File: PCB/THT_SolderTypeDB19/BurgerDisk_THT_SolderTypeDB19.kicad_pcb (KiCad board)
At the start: 2 copper layers, 93.7 x 67.6 mm, 18 parts, among them J1 Daisy port in, J2 MicroSD module, J3 UART, J4 Daisy port out, U1 PC817

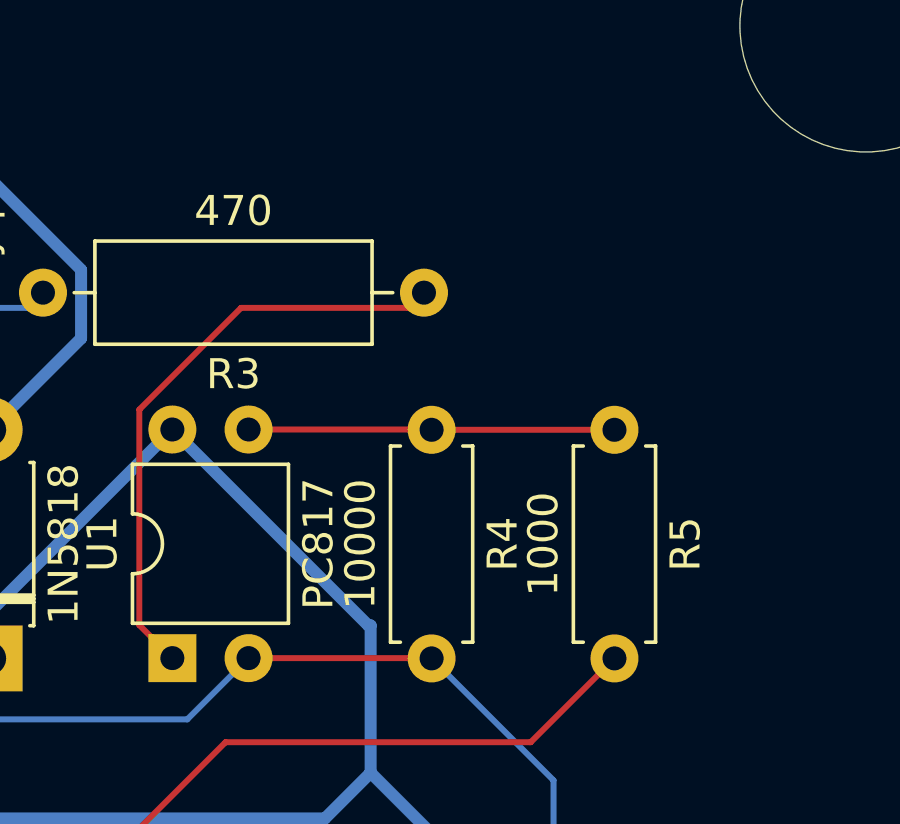
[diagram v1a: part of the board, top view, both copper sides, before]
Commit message: Reverse 3 resistors for correct silkscreen orientation
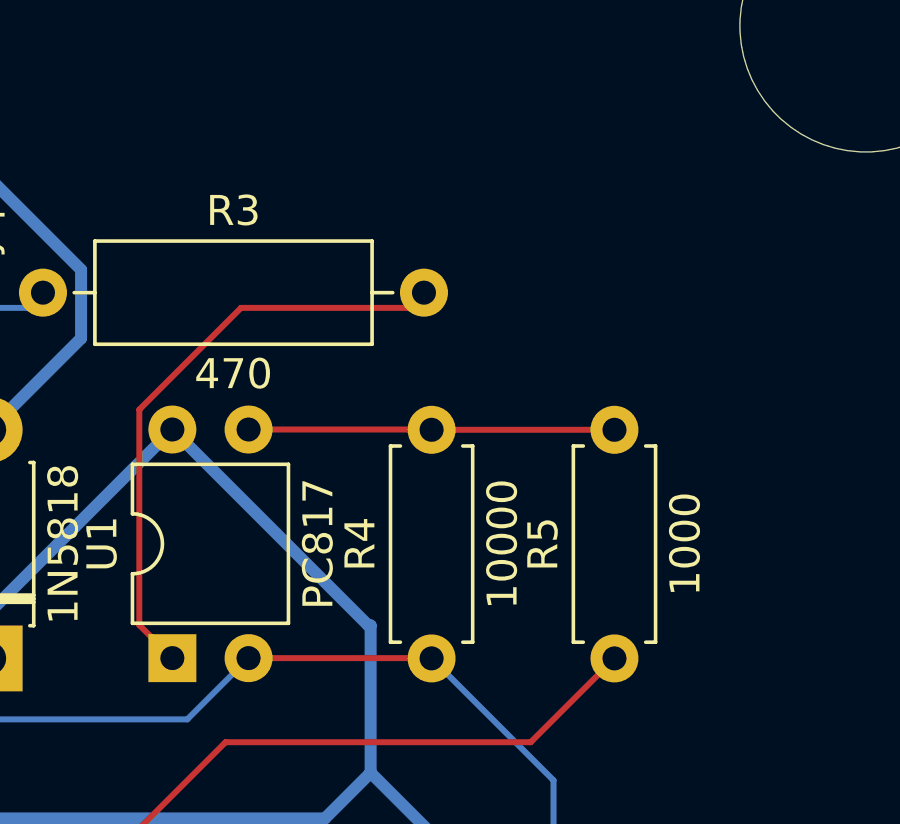
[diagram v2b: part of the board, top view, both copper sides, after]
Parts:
- moved R3 12.7 mm to (126.7, 72.9), turned to 0 degrees
- moved R4 7.62 mm to (139.7, 85.1), turned to 90 degrees
- moved R5 7.62 mm to (145.8, 85.1), turned to 90 degrees
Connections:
- R3 pad 1: Net-(R3-Pad1) -> DRV2_in
- R3 pad 2: DRV2_in -> Net-(R3-Pad2)
- R4 pad 1: Net-(R4-Pad1) -> GND
- R4 pad 2: GND -> Net-(R4-Pad2)
- R5 pad 1: Net-(R4-Pad1) -> DRV2_burgerDisk
- R5 pad 2: DRV2_burgerDisk -> Net-(R4-Pad2)
- U1 pad 1: Net-(R3-Pad1) -> Net-(R3-Pad2)
- U1 pad 3: Net-(R4-Pad1) -> Net-(R4-Pad2)
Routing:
- net Net-(R3-Pad2): track 0.00 -> 19.8 mm
- net Net-(R3-Pad1): track 19.8 -> 0.00 mm
- net Net-(R4-Pad2): track 0.00 -> 12.2 mm
- net Net-(R4-Pad1): track 12.2 -> 0.00 mm
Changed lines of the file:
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@@
   (net 36 "unconnected-(A1-A6-Pad25)")
   (net 37 "unconnected-(A1-3V3-Pad17)")
-  (net 38 "Net-(R4-Pad1)")
-  (net 39 "Net-(R3-Pad1)")
+  (net 38 "Net-(R3-Pad2)")
+  (net 39 "Net-(R4-Pad2)")
   (net 40 "HDSEL_in")
   (net 41 "Net-(D4-A)")
@@
       (stroke (width 0.1) (type solid)) (layer "F.Fab"))
     (pad "1" thru_hole rect (at 0 0 90) (size 1.6 1.6) (drill 0.8) (layers "*.Cu" "*.Mask")
-      (net 39 "Net-(R3-Pad1)") (pintype "passive"))
+      (net 38 "Net-(R3-Pad2)") (pintype "passive"))
     (pad "2" thru_hole oval (at 0 2.54 90) (size 1.6 1.6) (drill 0.8) (layers "*.Cu" "*.Mask")
       (net 2 "GND") (pintype "passive"))
     (pad "3" thru_hole oval (at 7.62 2.54 90) (size 1.6 1.6) (drill 0.8) (layers "*.Cu" "*.Mask")
-      (net 38 "Net-(R4-Pad1)") (pintype "passive"))
+      (net 39 "Net-(R4-Pad2)") (pintype "passive"))
     (pad "4" thru_hole oval (at 7.62 0 90) (size 1.6 1.6) (drill 0.8) (layers "*.Cu" "*.Mask")
       (net 20 "5V_burgerDisk") (pintype "passive"))
@@
   )
   (footprint "Resistor_THT:R_Axial_DIN0309_L9.0mm_D3.2mm_P12.70mm_Horizontal" (layer "F.Cu")
-    (at 139.446 72.898 180)
+    (at 126.746 72.898)
     (descr "Resistor, Axial_DIN0309 series, Axial, Horizontal, pin pitch=12.7mm, 0.5W = 1/2W, length*diameter=9*3.2mm^2, http://cdn-reichelt.de/documents/datenblatt/B400/1_4W%23YAG.pdf")
     (tags "Resistor Axial_DIN0309 series Axial Horizontal pin pitch 12.7mm 0.5W = 1/2W length 9mm diameter 3.2mm")
@@
     (fp_line (start 12.7 0) (end 10.85 0)
       (stroke (width 0.1) (type solid)) (layer "F.Fab"))
-    (pad "1" thru_hole circle (at 0 0 180) (size 1.6 1.6) (drill 0.8) (layers "*.Cu" "*.Mask")
-      (net 39 "Net-(R3-Pad1)") (pintype "passive"))
-    (pad "2" thru_hole oval (at 12.7 0 180) (size 1.6 1.6) (drill 0.8) (layers "*.Cu" "*.Mask")
+    (pad "1" thru_hole circle (at 0 0) (size 1.6 1.6) (drill 0.8) (layers "*.Cu" "*.Mask")
       (net 27 "DRV2_in") (pintype "passive"))
+    (pad "2" thru_hole oval (at 12.7 0) (size 1.6 1.6) (drill 0.8) (layers "*.Cu" "*.Mask")
+      (net 38 "Net-(R3-Pad2)") (pintype "passive"))
     (model "${KICAD6_3DMODEL_DIR}/Resistor_THT.3dshapes/R_Axial_DIN0309_L9.0mm_D3.2mm_P12.70mm_Horizontal.wrl"
       (offset (xyz 0 0 0))
@@
   )
   (footprint "Resistor_THT:R_Axial_DIN0207_L6.3mm_D2.5mm_P7.62mm_Horizontal" (layer "F.Cu")
-    (at 139.7 77.47 -90)
+    (at 139.7 85.09 90)
     (descr "Resistor, Axial_DIN0207 series, Axial, Horizontal, pin pitch=7.62mm, 0.25W = 1/4W, length*diameter=6.3*2.5mm^2, http://cdn-reichelt.de/documents/datenblatt/B400/1_4W%23YAG.pdf")
     (tags "Resistor Axial_DIN0207 series Axial Horizontal pin pitch 7.62mm 0.25W = 1/4W length 6.3mm diameter 2.5mm")
@@
     (fp_line (start 7.62 0) (end 6.96 0)
       (stroke (width 0.1) (type solid)) (layer "F.Fab"))
-    (pad "1" thru_hole circle (at 0 0 270) (size 1.6 1.6) (drill 0.8) (layers "*.Cu" "*.Mask")
-      (net 38 "Net-(R4-Pad1)") (pintype "passive"))
-    (pad "2" thru_hole oval (at 7.62 0 270) (size 1.6 1.6) (drill 0.8) (layers "*.Cu" "*.Mask")
+    (pad "1" thru_hole circle (at 0 0 90) (size 1.6 1.6) (drill 0.8) (layers "*.Cu" "*.Mask")
       (net 2 "GND") (pintype "passive"))
+    (pad "2" thru_hole oval (at 7.62 0 90) (size 1.6 1.6) (drill 0.8) (layers "*.Cu" "*.Mask")
+      (net 39 "Net-(R4-Pad2)") (pintype "passive"))
     (model "${KICAD6_3DMODEL_DIR}/Resistor_THT.3dshapes/R_Axial_DIN0207_L6.3mm_D2.5mm_P7.62mm_Horizontal.wrl"
       (offset (xyz 0 0 0))
@@
   )
   (footprint "Resistor_THT:R_Axial_DIN0207_L6.3mm_D2.5mm_P7.62mm_Horizontal" (layer "F.Cu")
-    (at 145.796 77.47 -90)
+    (at 145.796 85.09 90)
     (descr "Resistor, Axial_DIN0207 series, Axial, Horizontal, pin pitch=7.62mm, 0.25W = 1/4W, length*diameter=6.3*2.5mm^2, http://cdn-reichelt.de/documents/datenblatt/B400/1_4W%23YAG.pdf")
     (tags "Resistor Axial_DIN0207 series Axial Horizontal pin pitch 7.62mm 0.25W = 1/4W length 6.3mm diameter 2.5mm")
@@
     (fp_line (start 7.62 0) (end 6.96 0)
       (stroke (width 0.1) (type solid)) (layer "F.Fab"))
-    (pad "1" thru_hole circle (at 0 0 270) (size 1.6 1.6) (drill 0.8) (layers "*.Cu" "*.Mask")
-      (net 38 "Net-(R4-Pad1)") (pintype "passive"))
-    (pad "2" thru_hole oval (at 7.62 0 270) (size 1.6 1.6) (drill 0.8) (layers "*.Cu" "*.Mask")
+    (pad "1" thru_hole circle (at 0 0 90) (size 1.6 1.6) (drill 0.8) (layers "*.Cu" "*.Mask")
       (net 10 "DRV2_burgerDisk") (pintype "passive"))
+    (pad "2" thru_hole oval (at 7.62 0 90) (size 1.6 1.6) (drill 0.8) (layers "*.Cu" "*.Mask")
+      (net 39 "Net-(R4-Pad2)") (pintype "passive"))
     (model "${KICAD6_3DMODEL_DIR}/Resistor_THT.3dshapes/R_Axial_DIN0207_L6.3mm_D2.5mm_P7.62mm_Horizontal.wrl"
       (offset (xyz 0 0 0))
@@
   (segment (start 139.192 50.8) (end 140.965 49.027) (width 0.2) (layer "B.Cu") (net 28))
   (segment (start 140.965 49.027) (end 140.965 45.72) (width 0.2) (layer "B.Cu") (net 28))
-  (segment (start 139.69 77.46) (end 139.7 77.47) (width 0.2) (layer "F.Cu") (net 38))
-  (segment (start 139.7 77.47) (end 145.796 77.47) (width 0.2) (layer "F.Cu") (net 38))
-  (segment (start 133.599 77.46) (end 139.69 77.46) (width 0.2) (layer "F.Cu") (net 38))
-  (segment (start 129.959 83.98) (end 129.959 76.797) (width 0.2) (layer "F.Cu") (net 39))
-  (segment (start 131.059 85.08) (end 129.959 83.98) (width 0.2) (layer "F.Cu") (net 39))
-  (segment (start 138.938 73.406) (end 139.446 72.898) (width 0.2) (layer "F.Cu") (net 39))
-  (segment (start 129.959 76.797) (end 133.35 73.406) (width 0.2) (layer "F.Cu") (net 39))
-  (segment (start 133.35 73.406) (end 138.938 73.406) (width 0.2) (layer "F.Cu") (net 39))
+  (segment (start 129.959 83.98) (end 129.959 76.797) (width 0.2) (layer "F.Cu") (net 38))
+  (segment (start 131.059 85.08) (end 129.959 83.98) (width 0.2) (layer "F.Cu") (net 38))
+  (segment (start 138.938 73.406) (end 139.446 72.898) (width 0.2) (layer "F.Cu") (net 38))
+  (segment (start 129.959 76.797) (end 133.35 73.406) (width 0.2) (layer "F.Cu") (net 38))
+  (segment (start 133.35 73.406) (end 138.938 73.406) (width 0.2) (layer "F.Cu") (net 38))
+  (segment (start 139.69 77.46) (end 139.7 77.47) (width 0.2) (layer "F.Cu") (net 39))
+  (segment (start 139.7 77.47) (end 145.796 77.47) (width 0.2) (layer "F.Cu") (net 39))
+  (segment (start 133.599 77.46) (end 139.69 77.46) (width 0.2) (layer "F.Cu") (net 39))
   (segment (start 108.458 68.834) (end 107.068 70.224) (width 0.2) (layer "B.Cu") (net 40))
   (segment (start 107.068 77.35) (end 107.442 77.724) (width 0.2) (layer "B.Cu") (net 40))
@@
     (connect_pads (clearance 0.5))
     (min_thickness 0.25) (filled_areas_thickness no)
-    (fill (thermal_gap 0.5) (thermal_bridge_width 0.5))
+    (fill yes (thermal_gap 0.5) (thermal_bridge_width 0.5))
     (polygon
       (pts

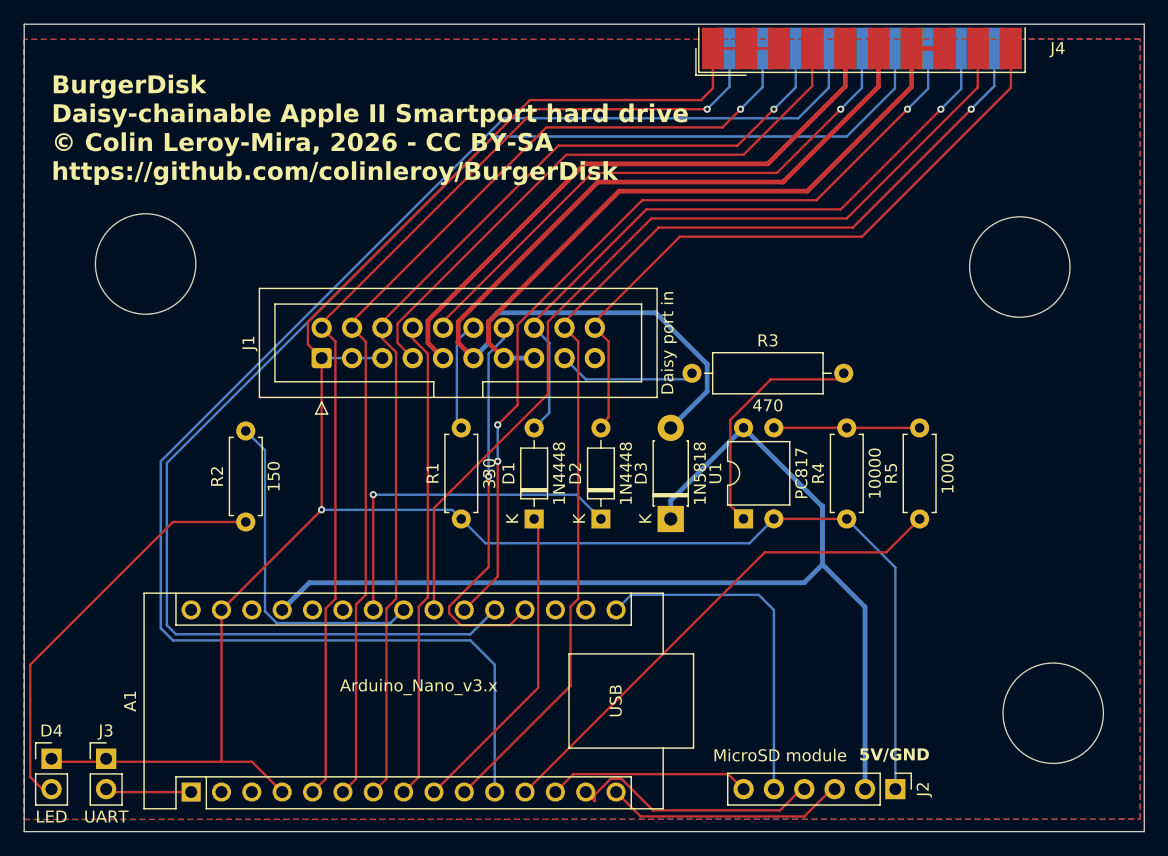
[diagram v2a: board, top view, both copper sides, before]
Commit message: Better routing to allow grounding to ground plane
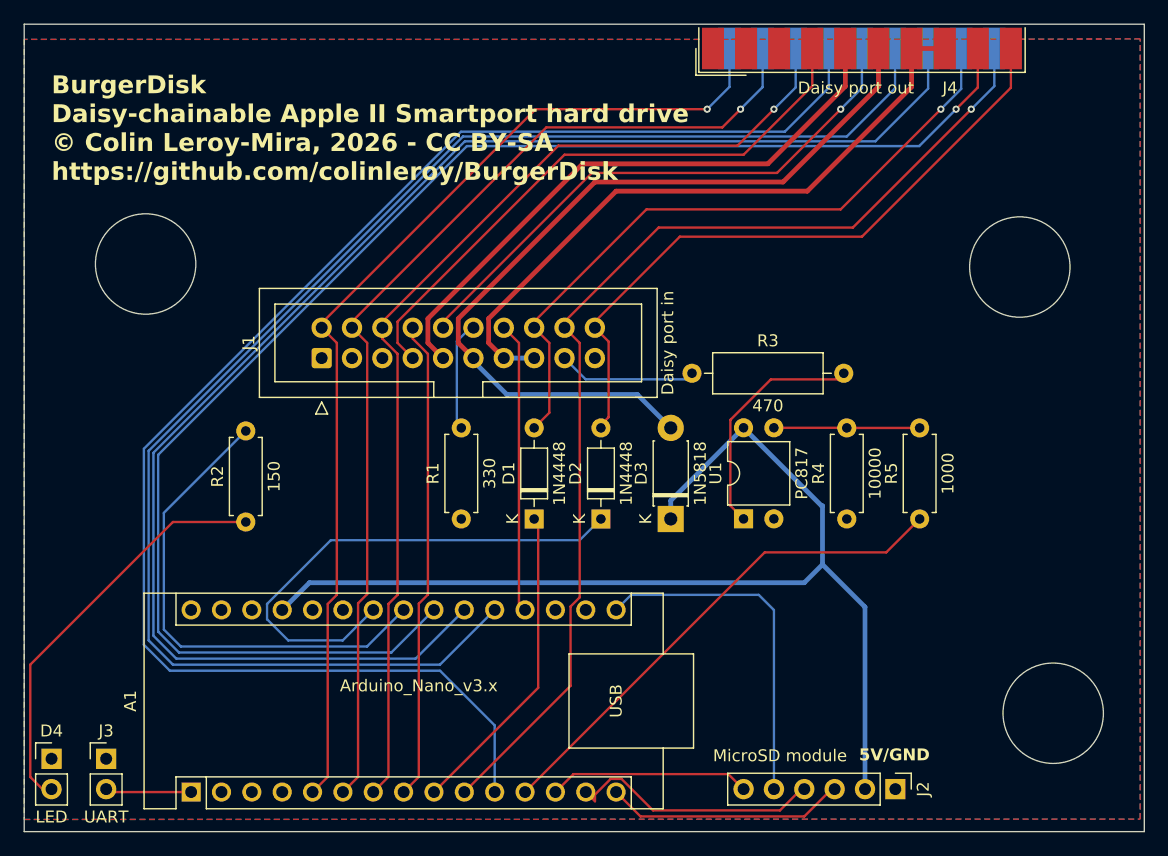
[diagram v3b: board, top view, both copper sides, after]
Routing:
- net GND: track 187.6 -> 0.01 mm, vias 1 -> 0
- net DRV1_out: track 71.6 -> 124.6 mm, vias 3 -> 0
- net DRV2_out: track 75.4 -> 124.7 mm, vias 0 -> 1
- net WRPROT_in: track 29.5 -> 42.8 mm, vias 1 -> 0
- net Net-(A1-A4): track 28.2 -> 41.4 mm
- net 5V_apple2: track 80.6 -> 69.3 mm
- net DRV1_in: track 33.1 -> 24.3 mm, vias 1 -> 0
- net HDSEL_out: track 119.4 -> 125.9 mm
- net PH3_out: track 126.0 -> 127.2 mm

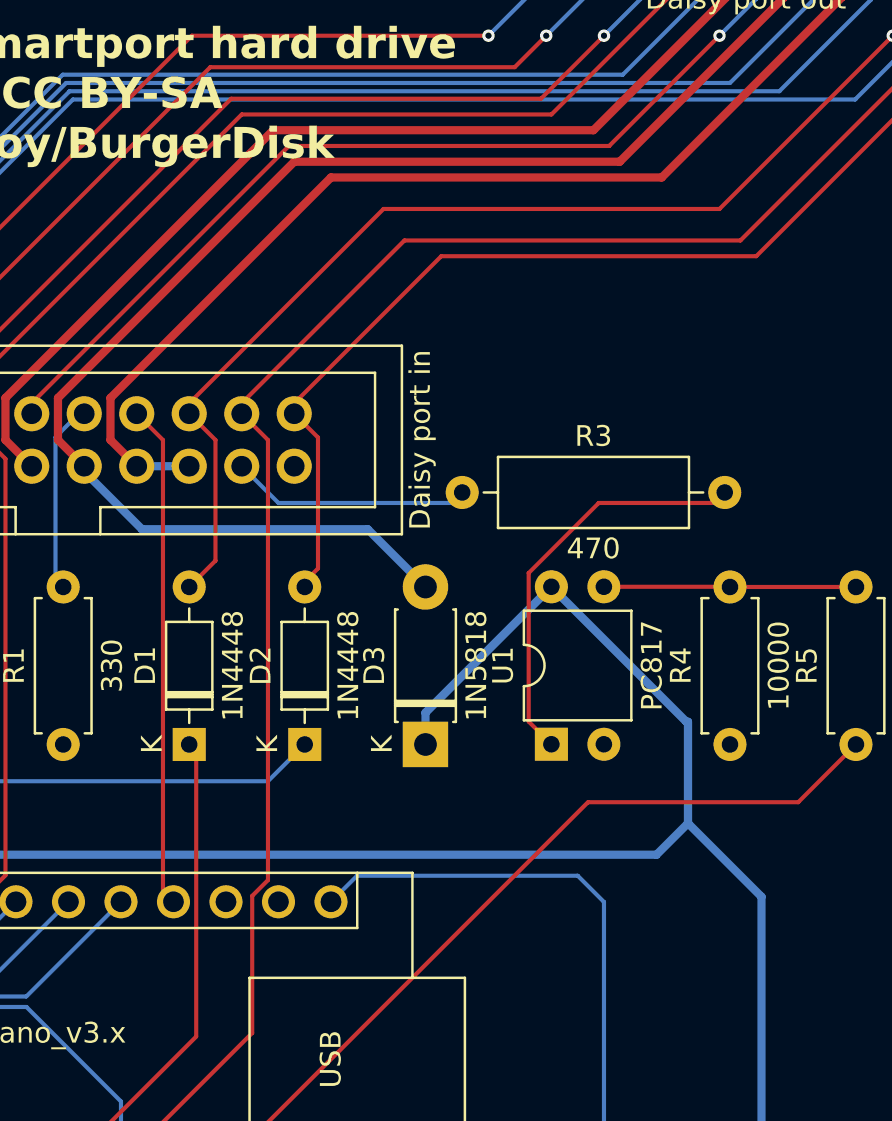
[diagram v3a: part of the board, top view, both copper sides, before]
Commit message: Remove RDDATA diode, causing harm on SoftSP
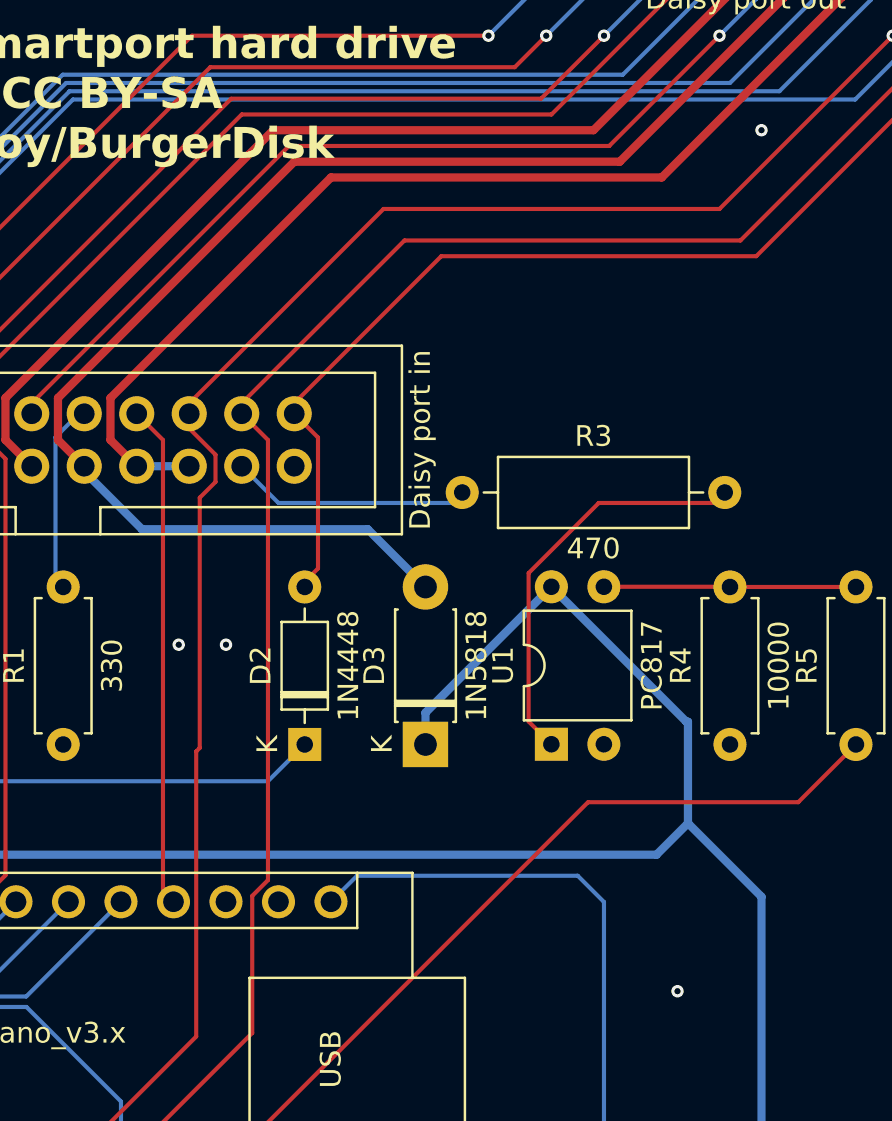
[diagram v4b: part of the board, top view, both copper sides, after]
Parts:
- removed D1: 1N4448, Diode_THT:D_DO-35_SOD27_P7.62mm_Horizontal
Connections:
- J1 pad 16: RDDATA_out -> RDDATA_in
- J4 pad 18: RDDATA_out -> RDDATA_in
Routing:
- net RDDATA_in: track 26.6 -> 91.1 mm, vias 0 -> 1
- net RDDATA_out: track 57.1 -> 0.00 mm, vias 1 -> 0
- net GND: vias 0 -> 4
